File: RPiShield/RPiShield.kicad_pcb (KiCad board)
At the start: 2 copper layers, 65 x 56.5 mm, 4 parts, among them J2 BBOX, J4 Corridor1, J7 FC68148, J8 2223

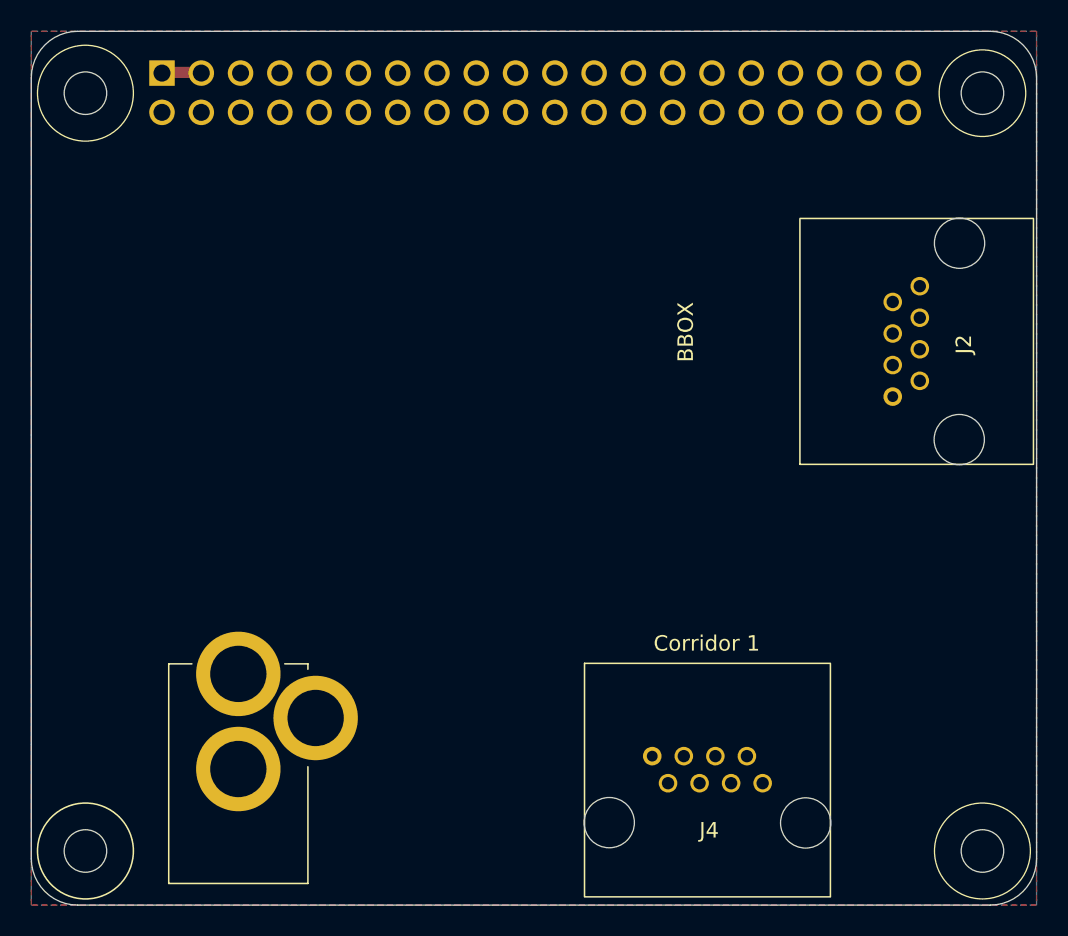
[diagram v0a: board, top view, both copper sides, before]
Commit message: Adding fuseholder to the HAT
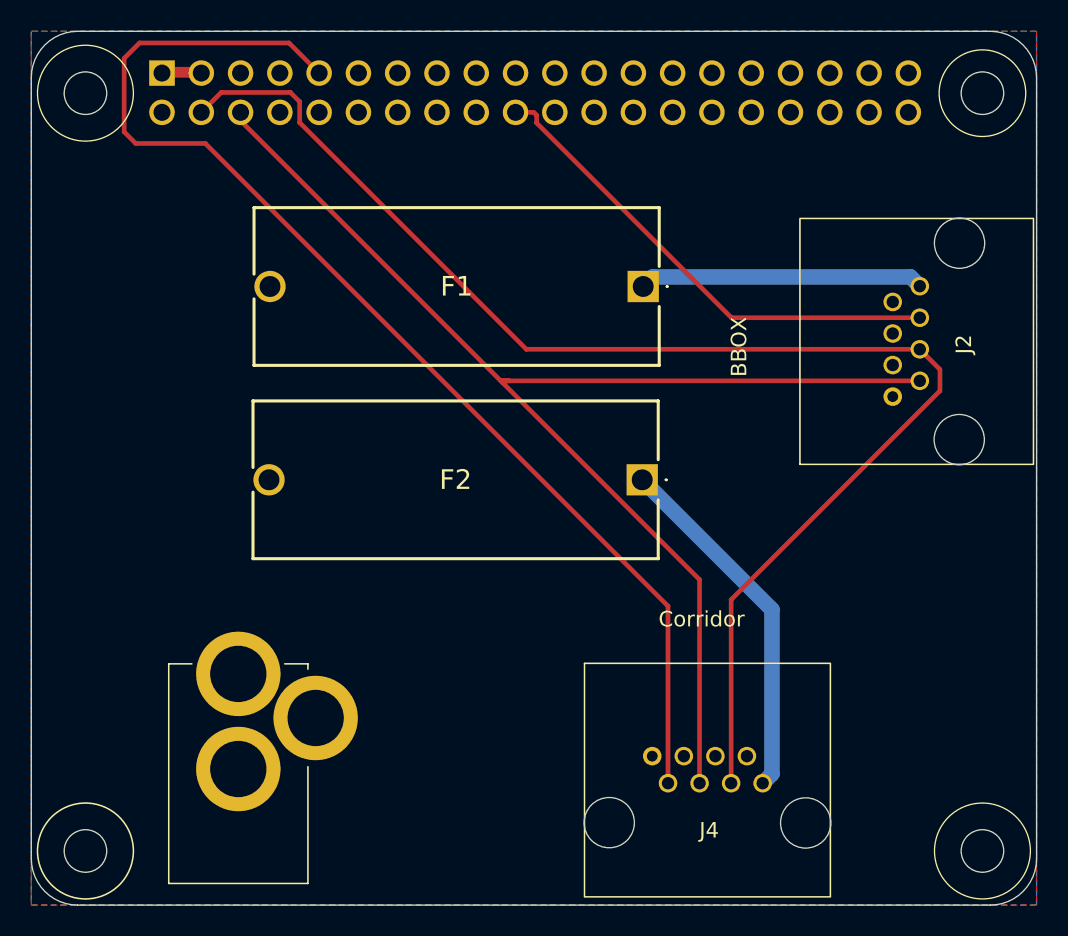
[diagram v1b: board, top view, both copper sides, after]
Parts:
- added F1: 05200101Z, 05200101Z:05200101Z, F.Cu at (169.1, 56.5)
- added F2: 05200101Z, 05200101Z:05200101Z, F.Cu at (169.0, 69.0)
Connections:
- J2 pad 8: +VDC -> Net-(F1-Pad1)
- J4 pad 8: +VDC -> Net-(F2-Pad1)
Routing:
- net I2C_SDA: track 0.00 -> 88.9 mm
- net I2C_SCL: track 0.49 -> 83.7 mm
- net RFID_TX: track 0.00 -> 77.9 mm
- net LED: track 0.00 -> 31.9 mm
- net Net-(F2-Pad1): track 0.00 -> 23.3 mm
- net Net-(F1-Pad1): track 0.00 -> 19.1 mm
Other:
- board text added: "Corridor"
- board text removed: "Corridor 1"
